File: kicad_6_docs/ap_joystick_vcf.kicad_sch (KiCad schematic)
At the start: 13 parts, among them J1 1/4"_jack, J2 1/4"_jack, U1 TL072

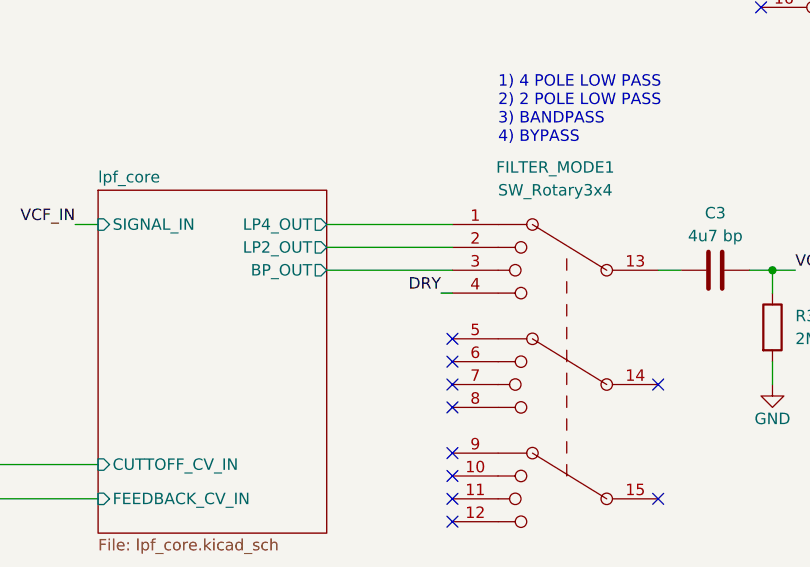
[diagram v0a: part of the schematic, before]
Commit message: fix VCF mode switch bypass position
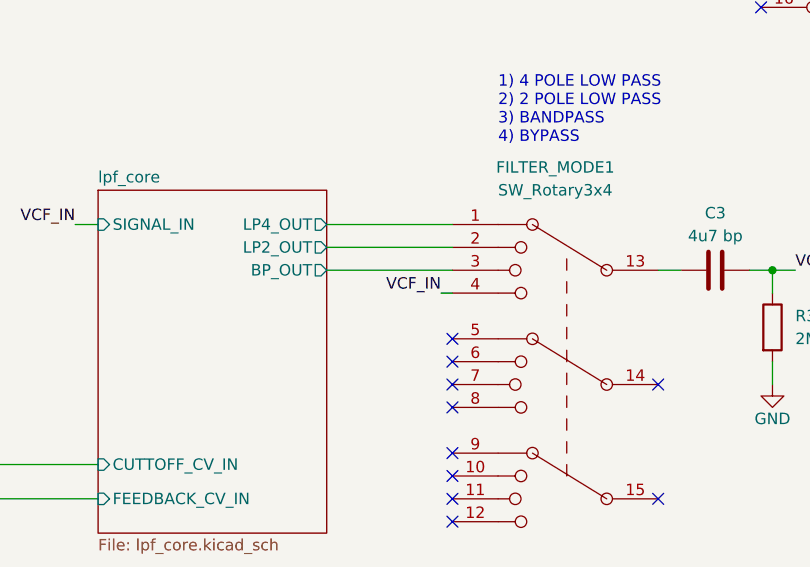
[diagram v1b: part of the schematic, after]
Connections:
- net DRY: no longer FILTER_MODE1.4
- net VCF_IN: now also FILTER_MODE1.4
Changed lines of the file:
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@@
     (effects (font (size 1.27 1.27)) (justify right bottom))
   )
-  (label "DRY" (at 119.38 101.6 180)
+  (label "VCF_IN" (at 119.38 101.6 180)
     (effects (font (size 1.27 1.27)) (justify right bottom))
   )

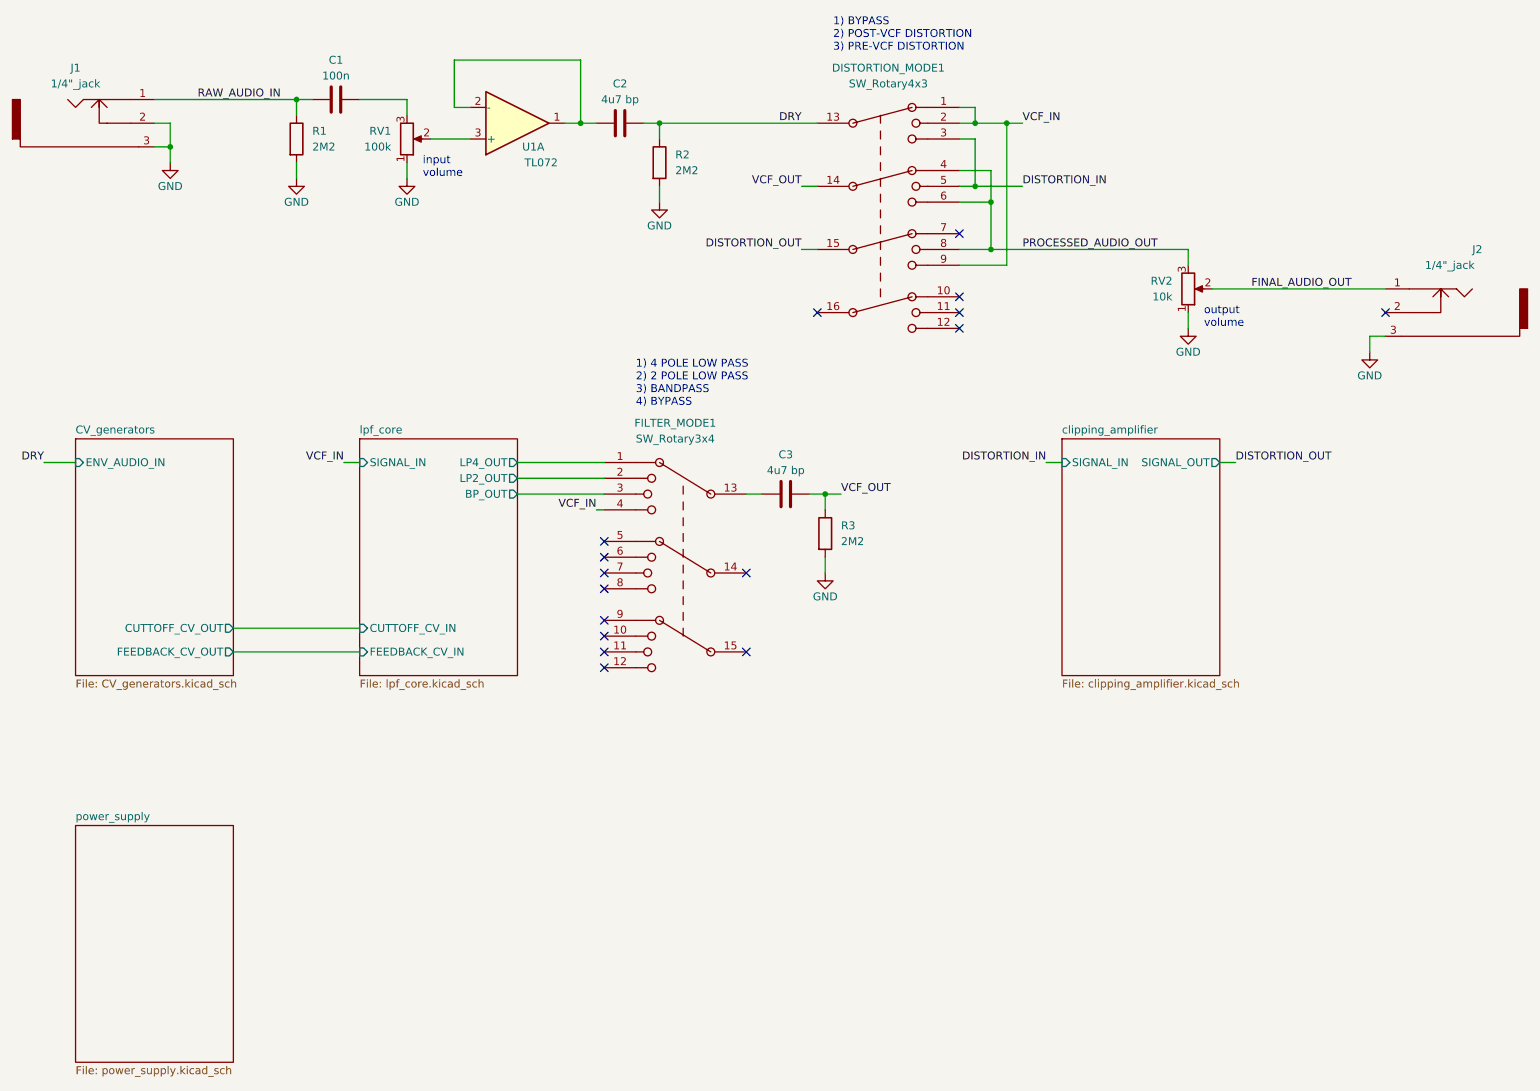
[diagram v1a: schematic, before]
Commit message: Fix power supply errors, tidy up schematic
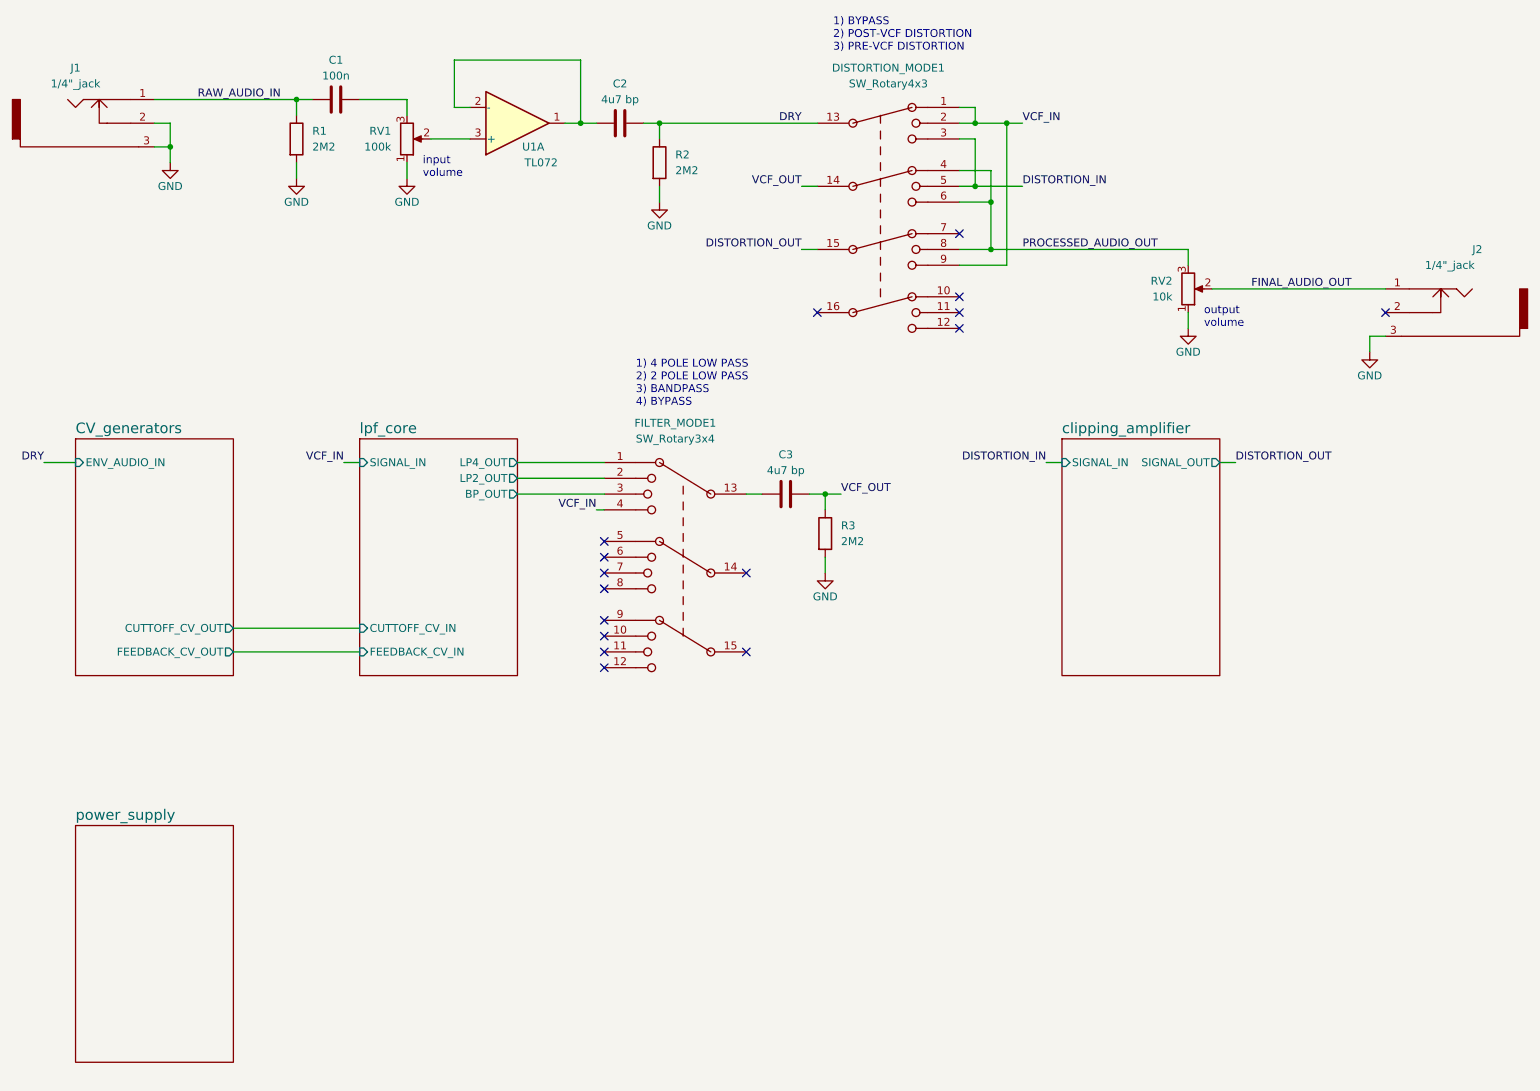
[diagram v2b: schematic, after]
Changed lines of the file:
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@@
   (title_block
     (title "A.P. Joystick VCF pedal")
-    (date "2022-01-14")
+    (date "2022-08-01")
     (rev "0")
     (comment 2 "creativecommons.org/licenses/by/4.0")
@@
     (pin "2")
     (pin "3")
+    (pin "5")
+    (pin "6")
+    (pin "7")
+    (pin "4")
+    (pin "8")
   )
   (symbol (lib_id "Device:R") (at 129.54 45.72 0) (unit 1)
@@
     (fill (color 0 0 0 0.0000))
     (property "Sheet name" "clipping_amplifier" (id 0) (at 194.31 89.4584 0)
-      (effects (font (size 1.27 1.27)) (justify left bottom))
+      (effects (font (size 1.7 1.7)) (justify left bottom))
     )
     (property "Sheet file" "clipping_amplifier.kicad_sch" (id 1) (at 194.31 128.8546 0)
-      (effects (font (size 1.27 1.27)) (justify left top))
+      (effects (font (size 1.27 1.27)) (justify left top) hide)
     )
     (pin "SIGNAL_OUT" output (at 219.71 93.98 0)
@@
     (fill (color 0 0 0 0.0000))
     (property "Sheet name" "power_supply" (id 0) (at 35.56 151.6884 0)
-      (effects (font (size 1.27 1.27)) (justify left bottom))
+      (effects (font (size 1.7 1.7)) (justify left bottom))
     )
     (property "Sheet file" "power_supply.kicad_sch" (id 1) (at 35.56 191.0846 0)
-      (effects (font (size 1.27 1.27)) (justify left top))
+      (effects (font (size 1.27 1.27)) (justify left top) hide)
     )
   )
@@
     (fill (color 0 0 0 0.0000))
     (property "Sheet name" "CV_generators" (id 0) (at 35.56 89.4584 0)
-      (effects (font (size 1.27 1.27)) (justify left bottom))
+      (effects (font (size 1.7 1.7)) (justify left bottom))
     )
     (property "Sheet file" "CV_generators.kicad_sch" (id 1) (at 35.56 128.8546 0)
-      (effects (font (size 1.27 1.27)) (justify left top))
+      (effects (font (size 1.27 1.27)) (justify left top) hide)
     )
     (pin "FEEDBACK_CV_OUT" output (at 60.96 124.46 0)
@@
     (fill (color 0 0 0 0.0000))
     (property "Sheet name" "lpf_core" (id 0) (at 81.28 89.4584 0)
-      (effects (font (size 1.27 1.27)) (justify left bottom))
+      (effects (font (size 1.7 1.7)) (justify left bottom))
     )
     (property "Sheet file" "lpf_core.kicad_sch" (id 1) (at 81.28 128.8546 0)
-      (effects (font (size 1.27 1.27)) (justify left top))
+      (effects (font (size 1.27 1.27)) (justify left top) hide)
     )
     (pin "SIGNAL_IN" input (at 81.28 93.98 180)
@@
     )
     (path "/4cab5afe-b810-46b3-94ba-f613dce05909/7871b063-34e6-43d7-bd79-505110a1d2cc"
-      (reference "RV5") (unit 1) (value "2k") (footprint "")
+      (reference "RV5") (unit 1) (value "5k") (footprint "")
     )
     (path "/4cab5afe-b810-46b3-94ba-f613dce05909/f9590ea8-434a-4c7a-96f5-c3a0c96cb1e0"
-      (reference "RV6") (unit 1) (value "2k") (footprint "")
+      (reference "RV6") (unit 1) (value "5k") (footprint "")
     )
     (path "/524434e5-0571-4b9e-8300-bfc332840f43/39bc48df-e09d-42c7-8c16-6c1219749369/d6cabb11-df3c-4ab0-ac00-855d95fd6bb5"
